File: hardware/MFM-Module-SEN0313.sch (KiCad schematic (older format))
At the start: 13 parts, among them J1 Program_conn, J2 Module board, J3 SEN0313 Header, Q1 Q_NMOS_GSD, Q2 Q_PMOS_GSD, SW1 PER_RESET, U1 ATtiny814-SS, U2 DS18B20

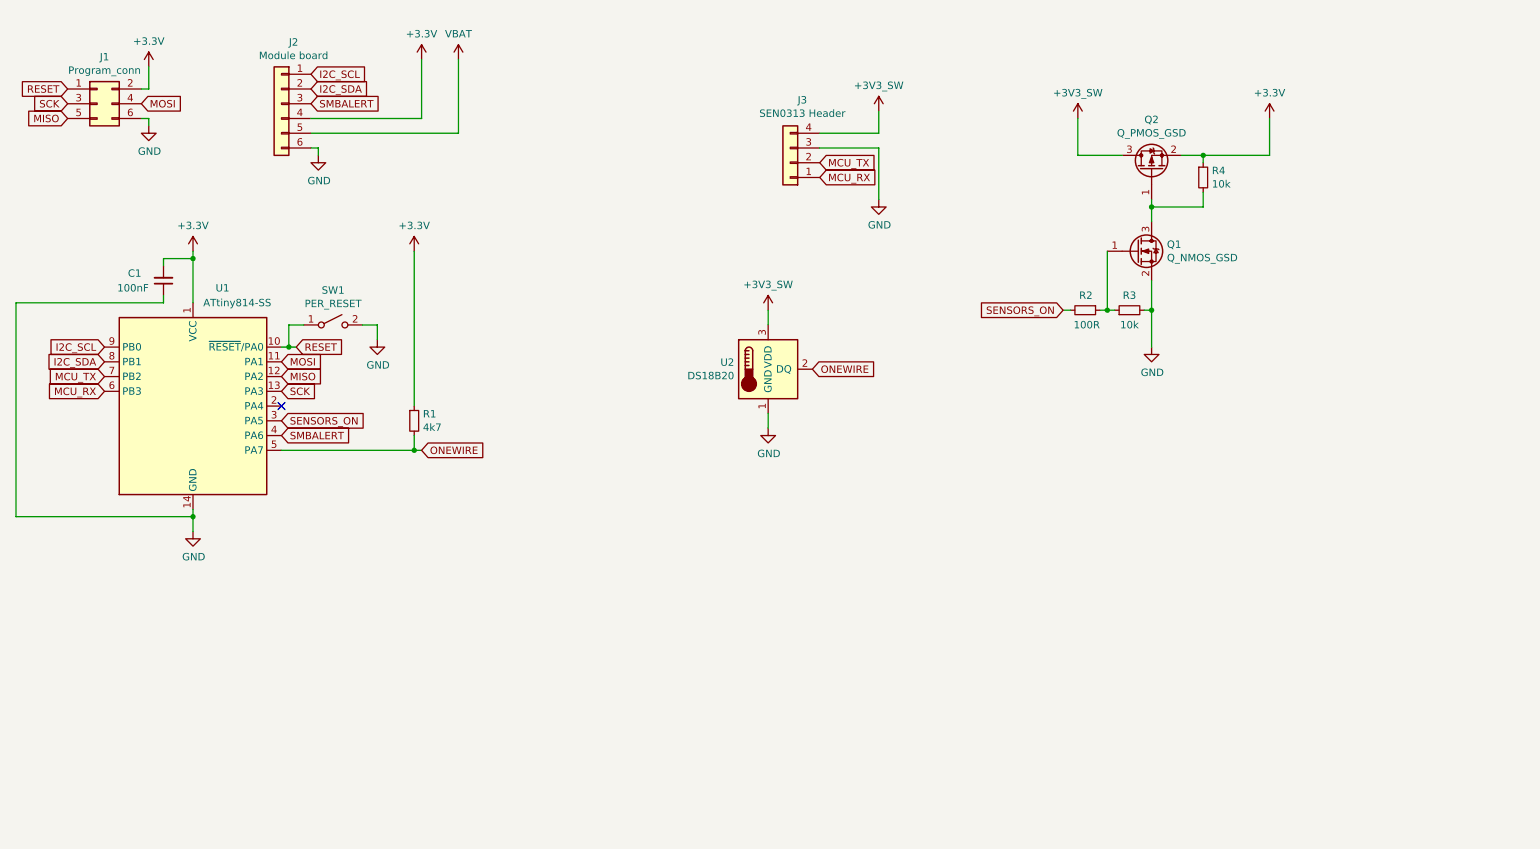
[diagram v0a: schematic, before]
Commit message: update BOM with production components. Updated PCB accordingly.
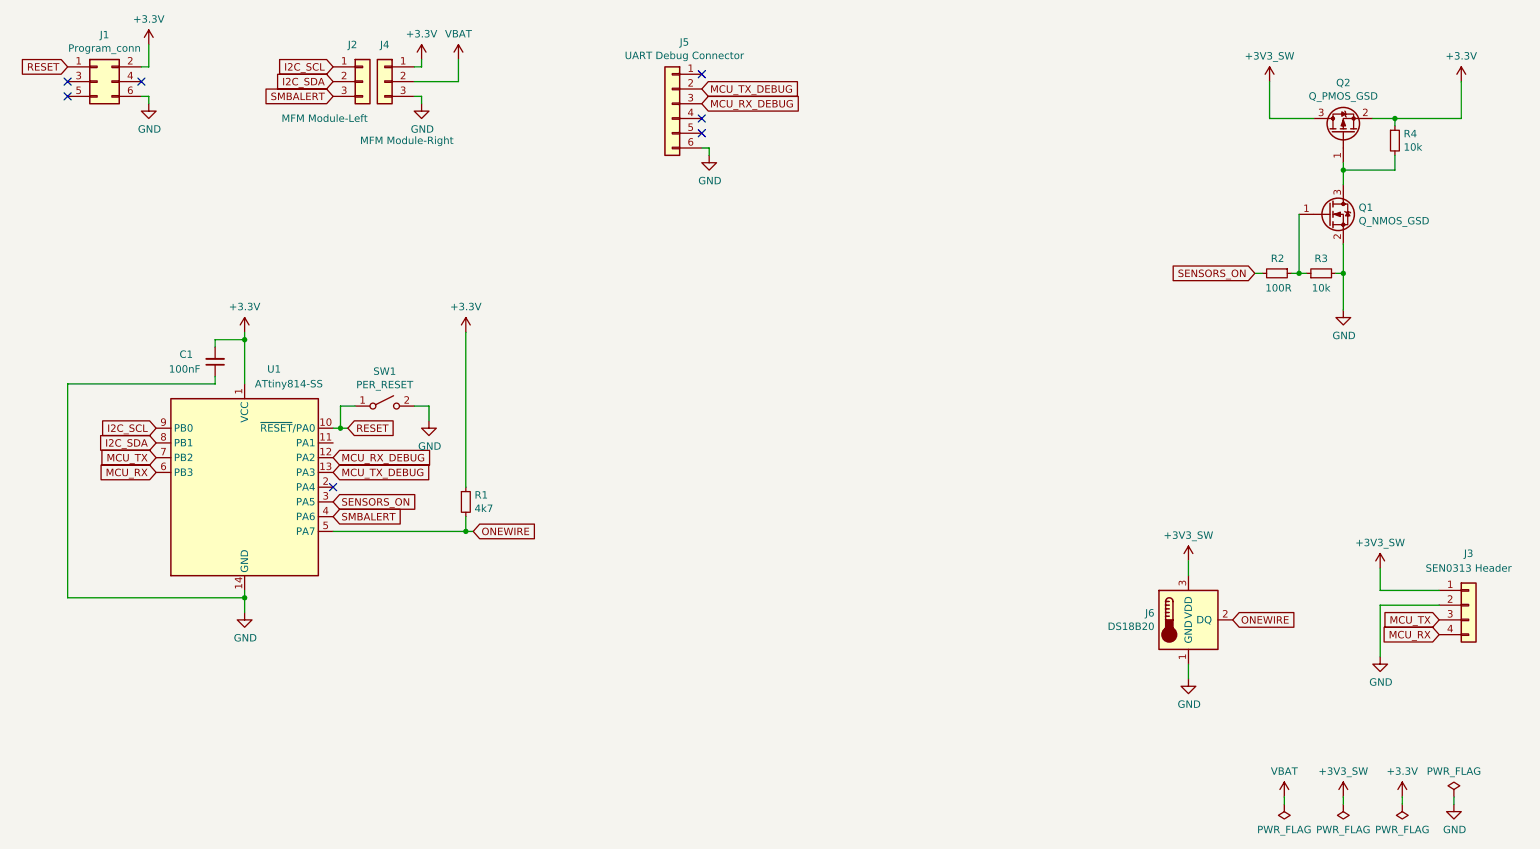
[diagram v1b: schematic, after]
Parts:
- removed J2: Module board, custom_library_FP:MFM_Module_Board, symbol Connector_Generic:Conn_01x06
- added J2: MFM Module-Left, custom_library_FP:MFM_Module_Board_P123, symbol Connector_Generic:Conn_01x03
- added J4: MFM Module-Right, Connector_PinSocket_2.54mm:PinSocket_1x03_P2.54mm_Vertical, symbol Connector_Generic:Conn_01x03
- added J5: UART Debug Connector, Connector_PinSocket_2.54mm:PinSocket_1x06_P2.54mm_Vertical, symbol Connector_Generic:Conn_01x06
- C1: MFR (none) -> TDK; MFR# (none) -> C1608X7R1E104K080AA
- J1: MFR (none) -> Preci-dip; MFR# (none) -> 892-18-006-10-001101
- J3: footprint custom_library_FP:JST_PA_S04B-PASK-2_1x04_P2.00mm_Horizontal -> Connector_JST:JST_PH_S4B-PH-K_1x04_P2.00mm_Horizontal; Distributor (none) -> https://nl.farnell.com/jst-japan-solderless-terminals/s4b-p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; MFR (none) -> JST (JAPAN SOLDERLESS TERMINALS); MFR# (none) -> S4B-PH-K-S (LF)(SN)
- J6: renamed from U2; Distributor (none) -> https://nl.farnell.com/jst-japan-solderless-terminals/s3b-x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; MFR (none) -> JST (JAPAN SOLDERLESS TERMINALS); MFR# (none) -> S3B-XH-A (LF)(SN)
- Q1: MFR (none) -> Vishay; MFR# (none) -> 2N7002-T1-GE3
- Q2: MFR (none) -> Vishay / Siliconix; MFR# (none) -> SI2333DDS-T1-BE3
- R1: LCSC C25999 -> C23162; LCSC_MFR# 0603WAJ0472T5E -> 0603WAF4701T5E; MFR (none) -> Vishay; MFR# (none) -> CRCW06034K70FKEA
- R2: MFR (none) -> Vishay / Dale; MFR# (none) -> CRCW0603100RFKEC
- R3, R4: MFR (none) -> Vishay; MFR# (none) -> CRCW060310K0FKEAC
- SW1: footprint custom_library_FP:SW_SPST_JLC -> custom_library_FP:SW_SPST_PTS636; LCSC_FOOTPRINT (none) -> custom_library_FP:SW_SPST_JLC; MFR (none) -> C&K; MFR# (none) -> PTS636 SM43 SMTR LFS
- U1: MFR (none) -> Microchip Technology / Atmel; MFR# (none) -> ATTINY814-SSNR
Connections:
- net +3V3: now also J4.1 (Pin_1); no longer J3.4 (Pin_4), J6.3 (VDD), Q2.3 (D)
- net GND: now also J3.2 (Pin_2), J4.3 (Pin_3), J5.6 (Pin_6); no longer J3.3 (Pin_3)
- net I2C_SCL: now also J2.1 (Pin_1)
- net I2C_SDA: now also J2.2 (Pin_2)
- net MCU_RX: now also J3.4 (Pin_4); no longer J3.1 (Pin_1)
- net MCU_TX: now also J3.3 (Pin_3); no longer J3.2 (Pin_2)
- net SMBALERT: now also J2.3 (Pin_3)
- net VBAT: now also J4.2 (Pin_2)
- net MISO: no longer names the net of J1.5 (Pin_5)
- net MISO: no longer U1.12 (PA2)
- net MOSI: no longer names the net of U1.11 (PA1)
- net MOSI: no longer J1.4 (Pin_4)
- net SCK: no longer names the net of J1.3 (Pin_3)
- net SCK: no longer U1.13 (PA3)
- new net +3V3_SW: J3.1 (Pin_1), J6.3 (VDD), Q2.3 (D)
- new net MCU_RX_DEBUG: J5.3 (Pin_3), U1.12 (PA2)
- new net MCU_TX_DEBUG: J5.2 (Pin_2), U1.13 (PA3)
- no-connect marks 1 -> 7
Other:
- moved on the sheet: C1, J1, J3, J6, Q1, Q2, R1, R2, R3, R4, SW1, U1

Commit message: ready for production (@Productronics)
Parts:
- removed U1: ATtiny814-SS, Package_SO:SOIC-14_3.9x8.7mm_P1.27mm, symbol MCU_Microchip_ATtiny:ATtiny814-SS
- added U1: ATtiny1614-SS, Package_SO:SOIC-14_3.9x8.7mm_P1.27mm, symbol MCU_Microchip_ATtiny:ATtiny1614-SS
- J1: MFR# 892-18-006-10-001101 -> 892-18-006-10-002101
- J2, J4: MFR# 801-87-003-10-005101 -> 801-87-003-53-001101
- J3: footprint Connector_JST:JST_PH_S4B-PH-K_1x04_P2.00mm_Horizontal -> custom_library_FP:JST_PA_S04B-PASK-2_1x04_P2.00mm_Horizontal
- Q2: MFR# SI2333DDS-T1-BE3 -> SI2315BDS-T1-E3
- R1: MFR# CRCW06034K70FKEA -> RCC06034K70FKEA
- R2: MFR# CRCW0603100RFKEC -> CRCW0603100RFKEAC
- R3, R4: MFR# CRCW060310K0FKEAC -> RCC060310K0FKEA
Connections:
- net +3V3: now also U1.1 (VCC)
- net GND: now also U1.14 (GND)
- net I2C_SCL: now also U1.9 (PB0)
- net I2C_SDA: now also U1.8 (PB1)
- net MCU_RX: now also U1.6 (PB3)
- net MCU_RX_DEBUG: now also U1.12 (PA2)
- net MCU_TX: now also U1.7 (PB2)
- net MCU_TX_DEBUG: now also U1.13 (PA3)
- net ONEWIRE: now also U1.5 (PA7)
- net RESET: now also U1.10 (~RESET~/PA0)
- net SENSORS_ON: now also U1.3 (PA5)
- net SMBALERT: now also U1.4 (PA6)
- no-connect marks 7 -> 10
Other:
- moved on the sheet: J3
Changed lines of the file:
@@
 Sheet 1 1
 Title "MFM Module SEN0313"
-Date "2021-05-24"
+Date "2021-10-09"
 Rev "V0.2"
-Comp "Senwize"
+Comp "Senwize B.V."
 Comment1 ""
 Comment2 ""
@@
 F 3 "~" H 1350 1150 50  0001 C CNN
 F 4 "Preci-dip" H 1350 1150 50  0001 C CNN "MFR"
-F 5 "892-18-006-10-001101" H 1350 1150 50  0001 C CNN "MFR#"
+F 5 "892-18-006-10-002101" H 1350 1150 50  0001 C CNN "MFR#"
 	1    1350 1150
 	1    0    0    -1
@@
 ONEWIRE
 NoConn ~ 2950 3900
-$Comp
-L Connector_Generic:Conn_01x04 J3
-U 1 1 60987959
-P 10650 4700
-F 0 "J3" H 10650 5050 50  0000 C CNN
-F 1 "SEN0313 Header" H 10650 4950 50  0000 C CNN
-F 2 "Connector_JST:JST_PH_S4B-PH-K_1x04_P2.00mm_Horizontal" H 10650 4700 50  0001 C CNN
-F 3 "~" H 10650 4700 50  0001 C CNN
-F 4 "https://nl.farnell.com/jst-japan-solderless-terminals/s4b-ph-k-s-lf-sn/header-tht-right-angle-2mm-4way/dp/9492488?st=jst%20ph%20s4b%20ph" H 10650 4700 50  0001 C CNN "Distributor"
-F 5 "JST (JAPAN SOLDERLESS TERMINALS)" H 10650 4700 50  0001 C CNN "MFR"
-F 6 "S4B-PH-K-S (LF)(SN)" H 10650 4700 50  0001 C CNN "MFR#"
-	1    10650 4700
-	1    0    0    -1
-$EndComp
 $Comp
 L Sensor_Temperature:DS18B20 J6
@@
 F 6 "0603WAF4701T5E" H 3850 4000 50  0001 C CNN "LCSC_MFR#"
 F 7 "Vishay" H 3850 4000 50  0001 C CNN "MFR"
-F 8 "CRCW06034K70FKEA" H 3850 4000 50  0001 C CNN "MFR#"
+F 8 "RCC06034K70FKEA" H 3850 4000 50  0001 C CNN "MFR#"
 	1    3850 4000
 	1    0    0    -1
@@
 P 3600 3450
 F 0 "#PWR010" H 3600 3200 50  0001 C CNN
-F 1 "GND" H 3605 3277 50  0000 C CNN
+F 1 "GND" H 3600 3300 50  0000 C CNN
 F 2 "" H 3600 3450 50  0001 C CNN
 F 3 "" H 3600 3450 50  0001 C CNN
@@
 Wire Wire Line
 	3850 2850 3850 3900
-$Comp
-L MCU_Microchip_ATtiny:ATtiny814-SS U1
-U 1 1 609B94E7
-P 2350 3900
-F 0 "U1" H 2550 4700 50  0000 C CNN
-F 1 "ATtiny814-SS" H 2650 4600 50  0000 C CNN
-F 2 "Package_SO:SOIC-14_3.9x8.7mm_P1.27mm" H 2350 3900 50  0001 C CIN
-F 3 "http://ww1.microchip.com/downloads/en/DeviceDoc/40001912A.pdf" H 2350 3900 50  0001 C CNN
-F 4 "Microchip Technology / Atmel" H 2350 3900 50  0001 C CNN "MFR"
-F 5 "ATTINY814-SSNR" H 2350 3900 50  0001 C CNN "MFR#"
-	1    2350 3900
-	1    0    0    -1
-$EndComp
 $Comp
 L Device:Q_PMOS_GSD Q2
@@
 F 5 "C10487" H 9800 1500 50  0001 C CNN "LCSC"
 F 6 "Vishay / Siliconix" H 9800 1500 50  0001 C CNN "MFR"
-F 7 "SI2333DDS-T1-BE3" H 9800 1500 50  0001 C CNN "MFR#"
+F 7 "SI2315BDS-T1-E3" H 9800 1500 50  0001 C CNN "MFR#"
 	1    9800 1500
 	0    -1   -1   0
@@
 F 6 "0603WAF1002T5E " H 10150 1550 50  0001 C CNN "LCSC_MFR#"
 F 7 "Vishay" H 10150 1550 50  0001 C CNN "MFR"
-F 8 "CRCW060310K0FKEAC" H 10150 1550 50  0001 C CNN "MFR#"
+F 8 "RCC060310K0FKEA" H 10150 1550 50  0001 C CNN "MFR#"
 	1    10150 1550
 	1    0    0    -1
@@
 F 6 "0603WAF1002T5E " H 9650 2450 50  0001 C CNN "LCSC_MFR#"
 F 7 "Vishay" H 9650 2450 50  0001 C CNN "MFR"
-F 8 "CRCW060310K0FKEAC" H 9650 2450 50  0001 C CNN "MFR#"
+F 8 "RCC060310K0FKEA" H 9650 2450 50  0001 C CNN "MFR#"
 	1    9650 2450
 	0    -1   -1   0
@@
 F 6 "0603WAJ0101T5E" H 9350 2450 50  0001 C CNN "LCSC_MFR#"
 F 7 "Vishay / Dale" H 9350 2450 50  0001 C CNN "MFR"
-F 8 "CRCW0603100RFKEC" H 9350 2450 50  0001 C CNN "MFR#"
+F 8 "CRCW0603100RFKEAC" H 9350 2450 50  0001 C CNN "MFR#"
 	1    9350 2450
 	0    1    1    0
@@
 Wire Wire Line
 	9200 2450 9250 2450
-Text GLabel 10450 4900 0    50   Input ~ 0
+Text GLabel 10500 4900 0    50   Input ~ 0
 MCU_RX
-Text GLabel 10450 4800 0    50   Input ~ 0
+Text GLabel 10500 4800 0    50   Input ~ 0
 MCU_TX
 Wire Wire Line
-	10050 4700 10450 4700
-Wire Wire Line
-	10050 4700 10050 5050
+	10100 4700 10500 4700
+Wire Wire Line
+	10100 4700 10100 5050
 $Comp
 L power:GND #PWR09
 U 1 1 60989746
-P 10050 5050
-F 0 "#PWR09" H 10050 4800 50  0001 C CNN
-F 1 "GND" H 10055 4877 50  0000 C CNN
-F 2 "" H 10050 5050 50  0001 C CNN
-F 3 "" H 10050 5050 50  0001 C CNN
-	1    10050 5050
-	1    0    0    -1
-$EndComp
-Wire Wire Line
-	10450 4600 10050 4600
-Wire Wire Line
-	10050 4450 10050 4600
+P 10100 5050
+F 0 "#PWR09" H 10100 4800 50  0001 C CNN
+F 1 "GND" H 10105 4877 50  0000 C CNN
+F 2 "" H 10100 5050 50  0001 C CNN
+F 3 "" H 10100 5050 50  0001 C CNN
+	1    10100 5050
+	1    0    0    -1
+$EndComp
+Wire Wire Line
+	10500 4600 10100 4600
+Wire Wire Line
+	10100 4450 10100 4600
 $Comp
 L Connector_Generic:Conn_01x03 J2
@@
 F 3 "~" H 3150 1150 50  0001 C CNN
 F 4 "Preci-dip" H 3150 1150 50  0001 C CNN "MFR"
-F 5 "801-87-003-10-005101" H 3150 1150 50  0001 C CNN "MFR#"
+F 5 "801-87-003-53-001101" H 3150 1150 50  0001 C CNN "MFR#"
 	1    3150 1150
 	1    0    0    -1
@@
 F 3 "~" H 3300 1150 50  0001 C CNN
 F 4 "Preci-dip" H 3300 1150 50  0001 C CNN "MFR"
-F 5 "801-87-003-10-005101" H 3300 1150 50  0001 C CNN "MFR#"
+F 5 "801-87-003-53-001101" H 3300 1150 50  0001 C CNN "MFR#"
 	1    3300 1150
 	-1   0    0    -1
@@
 L custom_library:+3V3_SW #PWR0102
 U 1 1 615597E4
-P 10050 4450
-F 0 "#PWR0102" H 10050 4300 50  0001 C CNN
-F 1 "+3V3_SW" H 10050 4623 50  0000 C CNN
-F 2 "" H 10050 4450 50  0001 C CNN
-F 3 "" H 10050 4450 50  0001 C CNN
-	1    10050 4450
+P 10100 4450
+F 0 "#PWR0102" H 10100 4300 50  0001 C CNN
+F 1 "+3V3_SW" H 10100 4623 50  0000 C CNN
+F 2 "" H 10100 4450 50  0001 C CNN
+F 3 "" H 10100 4450 50  0001 C CNN
+	1    10100 4450
 	1    0    0    -1
 $EndComp
@@
 Text GLabel 5450 1200 2    50   Input ~ 0
 MCU_TX_DEBUG
+$Comp
+L Connector_Generic:Conn_01x04 J3
+U 1 1 60987959
+P 10700 4700
+F 0 "J3" H 10700 5050 50  0000 C CNN
+F 1 "SEN0313 Header" H 10700 4950 50  0000 C CNN
+F 2 "custom_library_FP:JST_PA_S04B-PASK-2_1x04_P2.00mm_Horizontal" H 10700 4700 50  0001 C CNN
+F 3 "~" H 10700 4700 50  0001 C CNN
+F 4 "https://nl.farnell.com/jst-japan-solderless-terminals/s4b-ph-k-s-lf-sn/header-tht-right-angle-2mm-4way/dp/9492488?st=jst%20ph%20s4b%20ph" H 10700 4700 50  0001 C CNN "Distributor"
+F 5 "JST (JAPAN SOLDERLESS TERMINALS)" H 10700 4700 50  0001 C CNN "MFR"
+F 6 "S4B-PH-K-S (LF)(SN)" H 10700 4700 50  0001 C CNN "MFR#"
+	1    10700 4700
+	1    0    0    -1
+$EndComp
+$Comp
+L MCU_Microchip_ATtiny:ATtiny1614-SS U1
+U 1 1 610F1619
+P 2350 3900
+F 0 "U1" H 2350 4781 50  0000 C CNN
+F 1 "ATtiny1614-SS" H 2750 3200 50  0000 C CNN
+F 2 "Package_SO:SOIC-14_3.9x8.7mm_P1.27mm" H 2350 3900 50  0001 C CIN
+F 3 "http://ww1.microchip.com/downloads/en/DeviceDoc/ATtiny1614-data-sheet-40001995A.pdf" H 2350 3900 50  0001 C CNN
+F 4 "Microchip" H 2350 3900 50  0001 C CNN "MFR"
+F 5 "ATTINY1614-SSFR" H 2350 3900 50  0001 C CNN "MFR#"
+	1    2350 3900
+	1    0    0    -1
+$EndComp
+NoConn ~ 2950 3600
+NoConn ~ 5900 5500
+NoConn ~ 6100 3850
 $EndSCHEMATC
